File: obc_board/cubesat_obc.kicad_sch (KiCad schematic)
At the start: 16 parts

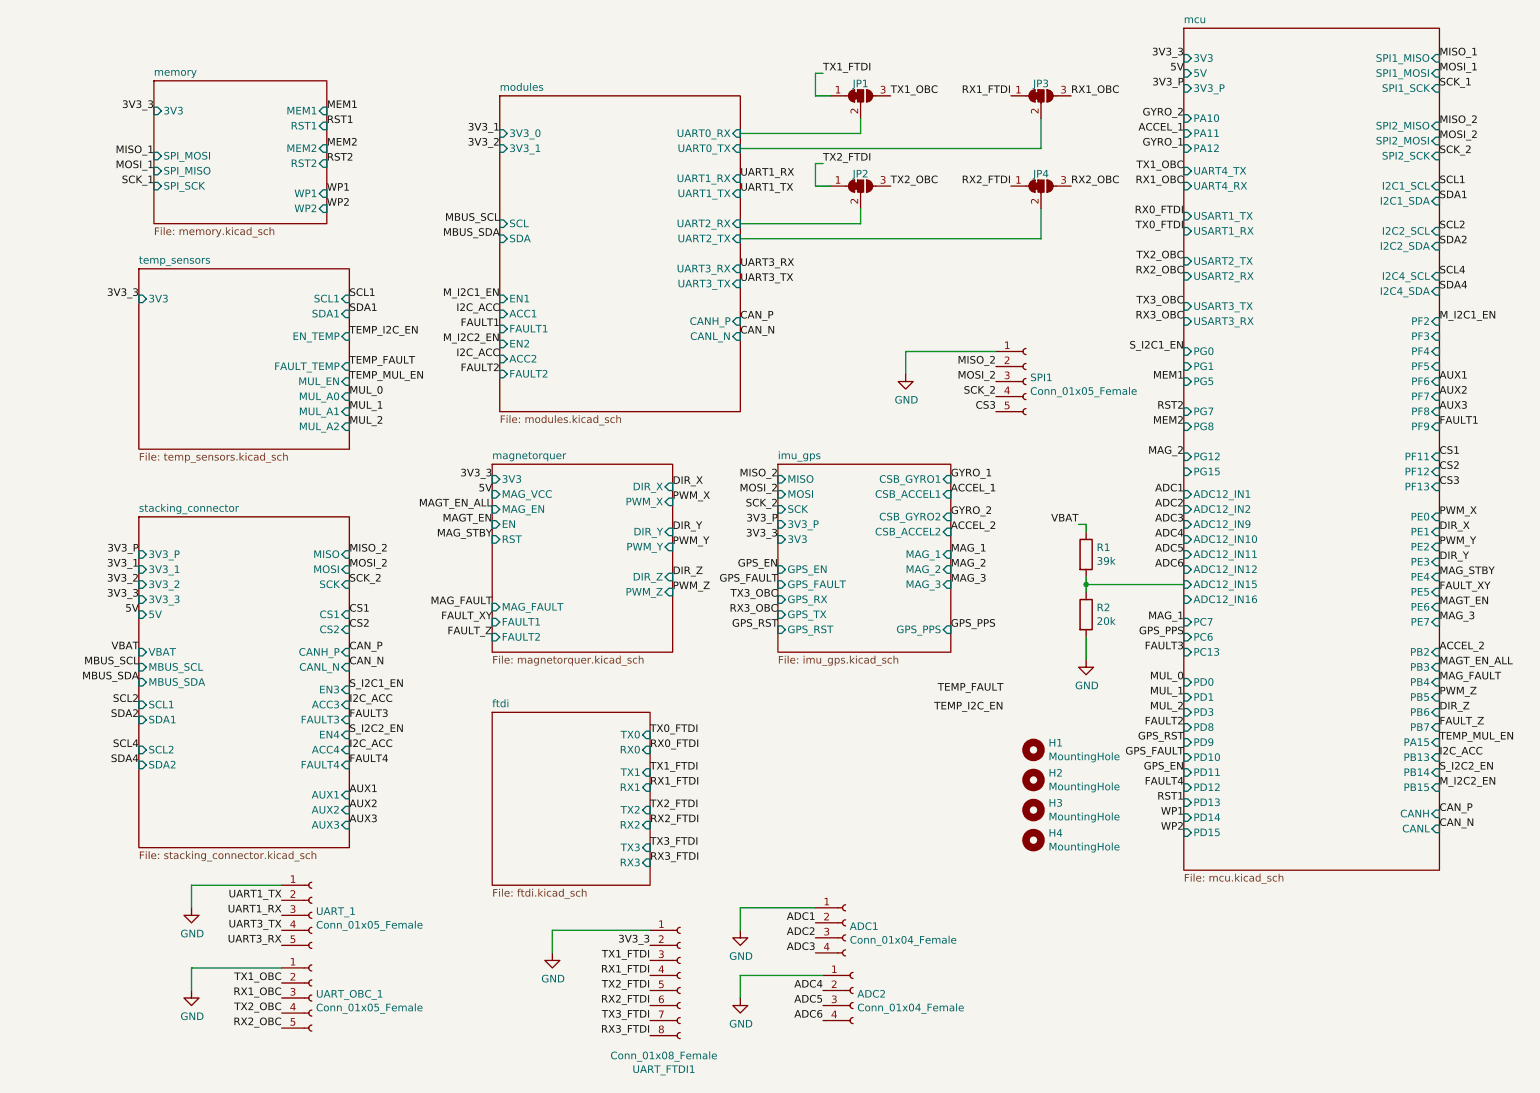
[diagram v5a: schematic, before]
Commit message: added silkscreen labels and gerber file
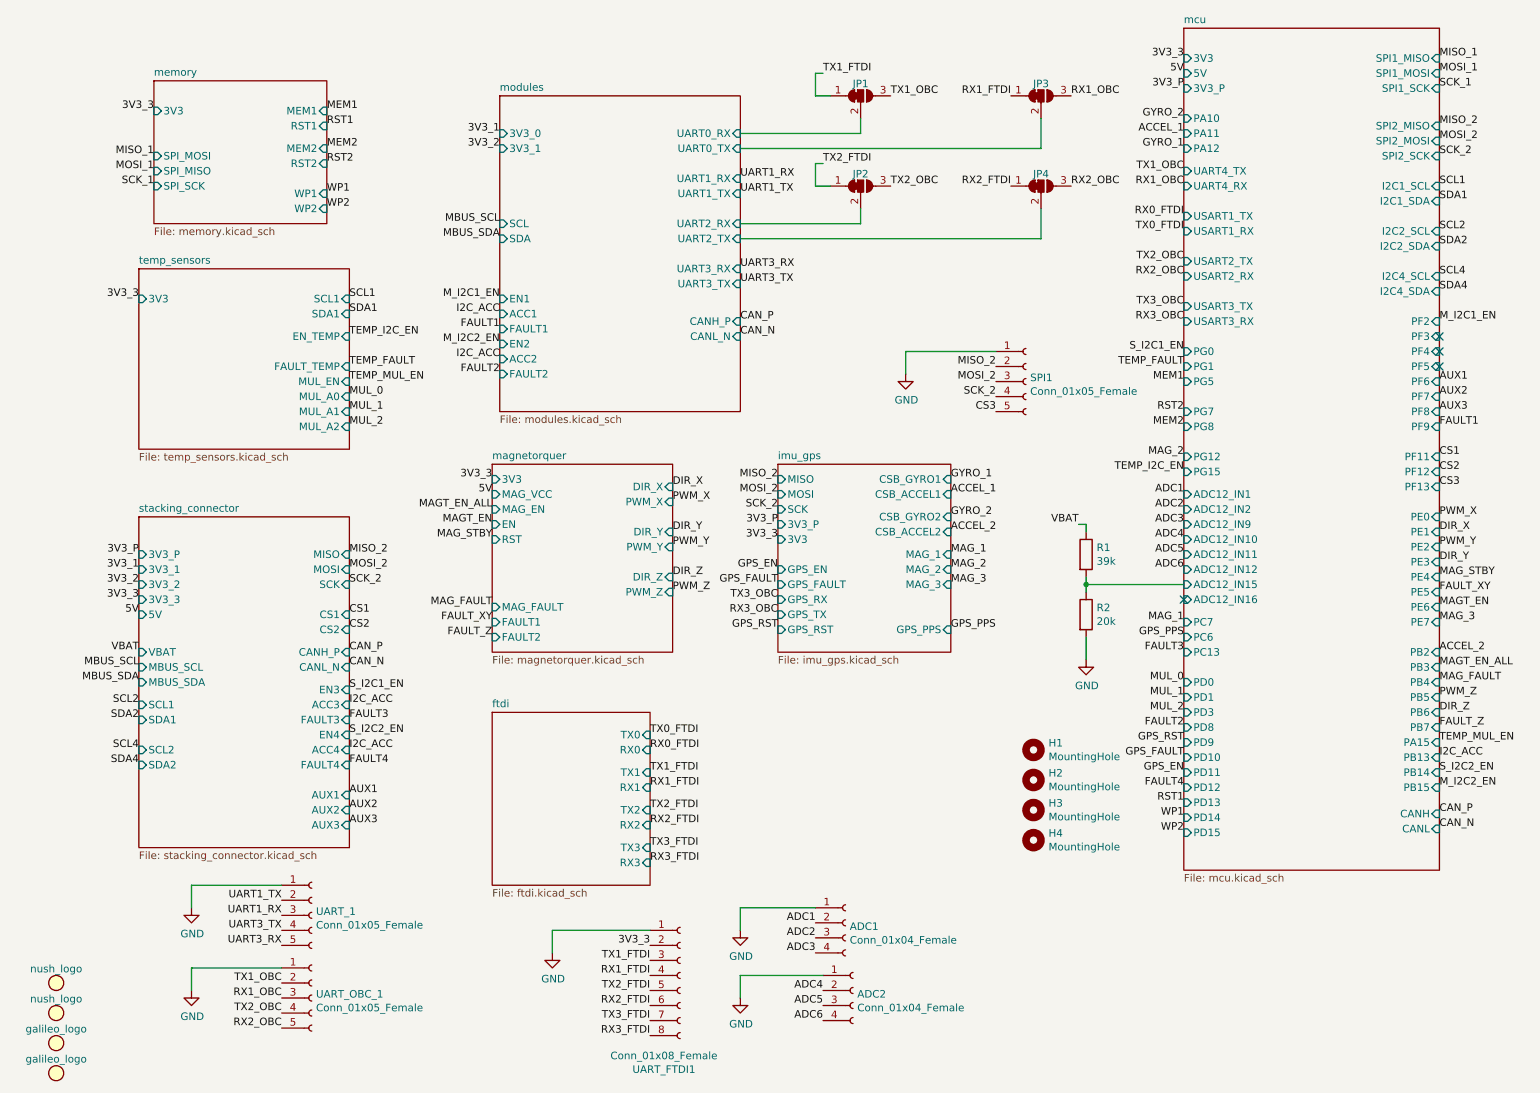
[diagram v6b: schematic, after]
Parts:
- added LOGO1, LOGO3: nush_logo, cubesat_obc:nush, symbol cubesat_obc_lib:nush_logo
- added LOGO2, LOGO4: galileo_logo, cubesat_obc:logo, symbol cubesat_obc_lib:galileo_logo
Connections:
- no-connect marks 0 -> 4
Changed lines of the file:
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@@
   (junction (at 194.31 111.76) (diameter 0) (color 0 0 0 0)
   )
+  (no_connect (at 210.82 114.3))
+  (no_connect (at 254 69.85))
+  (no_connect (at 254 72.39))
+  (no_connect (at 254 74.93))
   (wire (pts (xy 186.69 53.34) (xy 186.69 48.26))
     (stroke (width 0) (type default) (color 0 0 0 0))
@@
     (effects (font (size 1.27 1.27)) (justify right bottom))
   )
-  (label "TEMP_I2C_EN" (at 180.34 133.35 180)
+  (label "TEMP_I2C_EN" (at 210.82 92.71 180)
     (effects (font (size 1.27 1.27)) (justify right bottom))
   )
@@
     (effects (font (size 1.27 1.27)) (justify left bottom))
   )
-  (label "TEMP_FAULT" (at 180.34 130.175 180)
+  (label "TEMP_FAULT" (at 210.82 74.93 180)
     (effects (font (size 1.27 1.27)) (justify right bottom))
   )
@@
     (pin "1")
   )
+  (symbol (lib_id "cubesat_obc_lib:galileo_logo") (at 20.32 193.04 0) (unit 1)
+    (in_bom no) (on_board yes) (fields_autoplaced)
+    (property "Reference" "LOGO4" (id 0) (at 20.32 189.391 0)
+      (effects (font (size 1.27 1.27)) hide)
+    )
+    (property "Value" "galileo_logo" (id 1) (at 20.32 191.928 0))
+    (property "Footprint" "cubesat_obc:logo" (id 2) (at 20.32 193.04 0)
+      (effects (font (size 1.27 1.27)) hide)
+    )
+    (property "Datasheet" "" (id 3) (at 20.32 193.04 0)
+      (effects (font (size 1.27 1.27)) hide)
+    )
+  )
+  (symbol (lib_id "cubesat_obc_lib:galileo_logo") (at 20.32 187.96 0) (unit 1)
+    (in_bom no) (on_board yes) (fields_autoplaced)
+    (property "Reference" "LOGO2" (id 0) (at 20.32 184.311 0)
+      (effects (font (size 1.27 1.27)) hide)
+    )
+    (property "Value" "galileo_logo" (id 1) (at 20.32 186.848 0))
+    (property "Footprint" "cubesat_obc:logo" (id 2) (at 20.32 187.96 0)
+      (effects (font (size 1.27 1.27)) hide)
+    )
+    (property "Datasheet" "" (id 3) (at 20.32 187.96 0)
+      (effects (font (size 1.27 1.27)) hide)
+    )
+  )
   (symbol (lib_id "Jumper:SolderJumper_3_Bridged12") (at 186.69 44.45 0) (unit 1)
     (in_bom yes) (on_board yes) (fields_autoplaced)
@@
     )
     (pin "1")
+  )
+  (symbol (lib_id "cubesat_obc_lib:nush_logo") (at 20.32 176.53 0) (unit 1)
+    (in_bom no) (on_board yes) (fields_autoplaced)
+    (property "Reference" "LOGO3" (id 0) (at 20.32 174.151 0)
+      (effects (font (size 1.27 1.27)) hide)
+    )
+    (property "Value" "nush_logo" (id 1) (at 20.32 176.688 0))
+    (property "Footprint" "cubesat_obc:nush" (id 2) (at 20.32 176.53 0)
+      (effects (font (size 1.27 1.27)) hide)
+    )
+    (property "Datasheet" "" (id 3) (at 20.32 176.53 0)
+      (effects (font (size 1.27 1.27)) hide)
+    )
   )
   (symbol (lib_id "Connector:Conn_01x05_Female") (at 63.5 167.64 0) (unit 1)
@@
     )
     (pin "1")
+  )
+  (symbol (lib_id "cubesat_obc_lib:nush_logo") (at 20.32 181.61 0) (unit 1)
+    (in_bom no) (on_board yes) (fields_autoplaced)
+    (property "Reference" "LOGO1" (id 0) (at 20.32 179.231 0)
+      (effects (font (size 1.27 1.27)) hide)
+    )
+    (property "Value" "nush_logo" (id 1) (at 20.32 181.768 0))
+    (property "Footprint" "cubesat_obc:nush" (id 2) (at 20.32 181.61 0)
+      (effects (font (size 1.27 1.27)) hide)
+    )
+    (property "Datasheet" "" (id 3) (at 20.32 181.61 0)
+      (effects (font (size 1.27 1.27)) hide)
+    )
   )
   (symbol (lib_id "Connector:Conn_01x05_Female") (at 63.5 181.61 0) (unit 1)
@@
       (reference "L6") (unit 1) (value "4.7u") (footprint "cubesat_obc:L_Vishay_IHLP-2020")
     )
+    (path "/fd5bed97-1b44-4b26-b8b2-67238196ac4f"
+      (reference "LOGO1") (unit 1) (value "nush_logo") (footprint "cubesat_obc:nush")
+    )
+    (path "/2e22cb94-26aa-4819-a6b5-19b2eaba2a2a"
+      (reference "LOGO2") (unit 1) (value "galileo_logo") (footprint "cubesat_obc:logo")
+    )
+    (path "/c714194e-1b34-4b4e-883a-ced05fbeb8ae"
+      (reference "LOGO3") (unit 1) (value "nush_logo") (footprint "cubesat_obc:nush")
+    )
+    (path "/096e2b37-d7ae-49d5-8b8c-a245ea71385c"
+      (reference "LOGO4") (unit 1) (value "galileo_logo") (footprint "cubesat_obc:logo")
+    )
     (path "/00000000-0000-0000-0000-00005fc7207b/00000000-0000-0000-0000-00005fc87580"
       (reference "MAG_1") (unit 1) (value "Conn_01x02_Female") (footprint "Connector_Molex:Molex_PicoBlade_53261-0271_1x02-1MP_P1.25mm_Horizontal")
@@
       (reference "TP1") (unit 1) (value "MCO") (footprint "TestPoint:TestPoint_Pad_D1.5mm")
     )
+    (path "/00000000-0000-0000-0000-00005e7ec636/807784ee-2c9b-44bb-b95d-1f44a303a888"
+      (reference "TP?") (unit 1) (value "LSCO") (footprint "TestPoint:TestPoint_Pad_D1.5mm")
+    )
     (path "/00000000-0000-0000-0000-00005f315fb6/00000000-0000-0000-0000-00005f752a48"

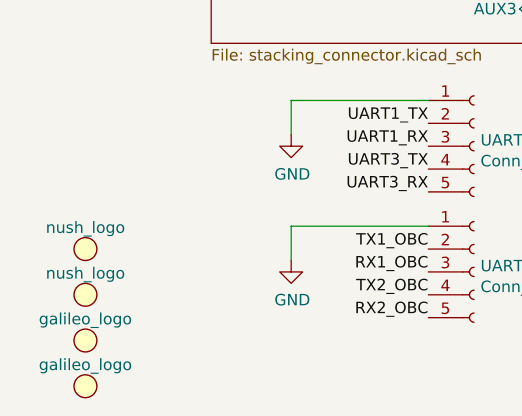
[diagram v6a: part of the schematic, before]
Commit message: added coordinate labels
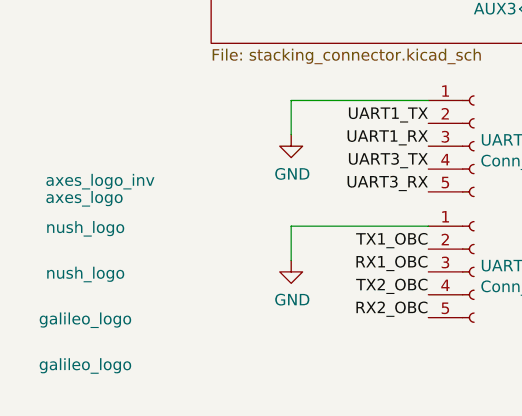
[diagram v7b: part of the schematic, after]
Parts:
- added LOGO5: axes_logo, cubesat_obc:axes, symbol cubesat_obc_lib:axes_logo
- added LOGO6: axes_logo_inv, cubesat_obc:axes_inv, symbol cubesat_obc_lib:axes_logo
- H1, H2, H3, H4, JP1, JP2, JP3, JP4: now left out of the parts list
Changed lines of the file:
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@@
   )
   (symbol (lib_id "Mechanical:MountingHole") (at 185.42 149.86 0) (unit 1)
-    (in_bom yes) (on_board yes)
+    (in_bom no) (on_board yes)
     (property "Reference" "H3" (id 0) (at 187.96 148.6916 0)
       (effects (font (size 1.27 1.27)) (justify left))
@@
   )
   (symbol (lib_id "Mechanical:MountingHole") (at 185.42 154.94 0) (unit 1)
-    (in_bom yes) (on_board yes)
+    (in_bom no) (on_board yes)
     (property "Reference" "H4" (id 0) (at 187.96 153.7716 0)
       (effects (font (size 1.27 1.27)) (justify left))
@@
   )
   (symbol (lib_id "Mechanical:MountingHole") (at 185.42 144.78 0) (unit 1)
-    (in_bom yes) (on_board yes)
+    (in_bom no) (on_board yes)
     (property "Reference" "H2" (id 0) (at 187.96 143.6116 0)
       (effects (font (size 1.27 1.27)) (justify left))
@@
   )
   (symbol (lib_id "Mechanical:MountingHole") (at 185.42 139.7 0) (unit 1)
-    (in_bom yes) (on_board yes)
+    (in_bom no) (on_board yes)
     (property "Reference" "H1" (id 0) (at 187.96 138.5316 0)
       (effects (font (size 1.27 1.27)) (justify left))
@@
     (pin "1")
   )
-  (symbol (lib_id "cubesat_obc_lib:galileo_logo") (at 20.32 193.04 0) (unit 1)
+  (symbol (lib_name "galileo_logo_1") (lib_id "cubesat_obc_lib:galileo_logo") (at 20.32 193.04 0) (unit 1)
     (in_bom no) (on_board yes) (fields_autoplaced)
     (property "Reference" "LOGO4" (id 0) (at 20.32 189.391 0)
@@
   )
   (symbol (lib_id "Jumper:SolderJumper_3_Bridged12") (at 186.69 44.45 0) (unit 1)
-    (in_bom yes) (on_board yes) (fields_autoplaced)
+    (in_bom no) (on_board yes) (fields_autoplaced)
     (property "Reference" "JP4" (id 0) (at 186.69 42.3982 0))
     (property "Value" "SolderJumper_3_Bridged12" (id 1) (at 186.69 42.3981 0)
@@
   )
   (symbol (lib_id "Jumper:SolderJumper_3_Bridged12") (at 156.21 44.45 0) (unit 1)
-    (in_bom yes) (on_board yes) (fields_autoplaced)
+    (in_bom no) (on_board yes) (fields_autoplaced)
     (property "Reference" "JP2" (id 0) (at 156.21 42.3982 0))
     (property "Value" "SolderJumper_3_Bridged12" (id 1) (at 156.21 42.3981 0)
@@
     (pin "3")
   )
+  (symbol (lib_id "cubesat_obc_lib:axes_logo") (at 20.32 173.355 0) (unit 1)
+    (in_bom no) (on_board yes)
+    (property "Reference" "LOGO5" (id 0) (at 21.59 172.0849 0)
+      (effects (font (size 1.27 1.27)) (justify left) hide)
+    )
+    (property "Value" "axes_logo" (id 1) (at 15.875 173.355 0)
+      (effects (font (size 1.27 1.27)) (justify left))
+    )
+    (property "Footprint" "cubesat_obc:axes" (id 2) (at 20.32 173.355 0)
+      (effects (font (size 1.27 1.27)) hide)
+    )
+    (property "Datasheet" "" (id 3) (at 20.32 173.355 0)
+      (effects (font (size 1.27 1.27)) hide)
+    )
+  )
   (symbol (lib_id "Jumper:SolderJumper_3_Bridged12") (at 156.21 29.21 0) (unit 1)
-    (in_bom yes) (on_board yes) (fields_autoplaced)
+    (in_bom no) (on_board yes) (fields_autoplaced)
     (property "Reference" "JP1" (id 0) (at 156.21 27.1582 0))
     (property "Value" "SolderJumper_3_Bridged12" (id 1) (at 156.21 27.1581 0)
@@
   )
   (symbol (lib_id "Jumper:SolderJumper_3_Bridged12") (at 186.69 29.21 0) (unit 1)
-    (in_bom yes) (on_board yes) (fields_autoplaced)
+    (in_bom no) (on_board yes) (fields_autoplaced)
     (property "Reference" "JP3" (id 0) (at 186.69 27.1582 0))
     (property "Value" "SolderJumper_3_Bridged12" (id 1) (at 186.69 27.1581 0)
@@
     (pin "1")
   )
-  (symbol (lib_id "cubesat_obc_lib:nush_logo") (at 20.32 176.53 0) (unit 1)
+  (symbol (lib_id "cubesat_obc_lib:axes_logo") (at 20.32 171.45 0) (unit 1)
+    (in_bom no) (on_board yes)
+    (property "Reference" "LOGO6" (id 0) (at 21.59 170.1799 0)
+      (effects (font (size 1.27 1.27)) (justify left) hide)
+    )
+    (property "Value" "axes_logo_inv" (id 1) (at 15.875 171.45 0)
+      (effects (font (size 1.27 1.27)) (justify left))
+    )
+    (property "Footprint" "cubesat_obc:axes_inv" (id 2) (at 20.32 171.45 0)
+      (effects (font (size 1.27 1.27)) hide)
+    )
+    (property "Datasheet" "" (id 3) (at 20.32 171.45 0)
+      (effects (font (size 1.27 1.27)) hide)
+    )
+  )
+  (symbol (lib_name "nush_logo_1") (lib_id "cubesat_obc_lib:nush_logo") (at 20.32 176.53 0) (unit 1)
     (in_bom no) (on_board yes) (fields_autoplaced)
     (property "Reference" "LOGO3" (id 0) (at 20.32 174.151 0)
@@
       (reference "LOGO4") (unit 1) (value "galileo_logo") (footprint "cubesat_obc:logo")
     )
+    (path "/4b138dbc-242e-4186-adee-f1b2ccf36379"
+      (reference "LOGO5") (unit 1) (value "axes_logo") (footprint "cubesat_obc:axes")
+    )
+    (path "/b98a0685-79cd-4074-bdb1-918f7563f4f8"
+      (reference "LOGO6") (unit 1) (value "axes_logo_inv") (footprint "cubesat_obc:axes_inv")
+    )
     (path "/00000000-0000-0000-0000-00005fc7207b/00000000-0000-0000-0000-00005fc87580"
       (reference "MAG_1") (unit 1) (value "Conn_01x02_Female") (footprint "Connector_Molex:Molex_PicoBlade_53261-0271_1x02-1MP_P1.25mm_Horizontal")
@@
     )
     (path "/00000000-0000-0000-0000-00005e7ec636/807784ee-2c9b-44bb-b95d-1f44a303a888"
-      (reference "TP?") (unit 1) (value "LSCO") (footprint "TestPoint:TestPoint_Pad_D1.5mm")
+      (reference "TP2") (unit 1) (value "LSCO") (footprint "TestPoint:TestPoint_Pad_D1.5mm")
     )
     (path "/00000000-0000-0000-0000-00005f315fb6/00000000-0000-0000-0000-00005f752a48"

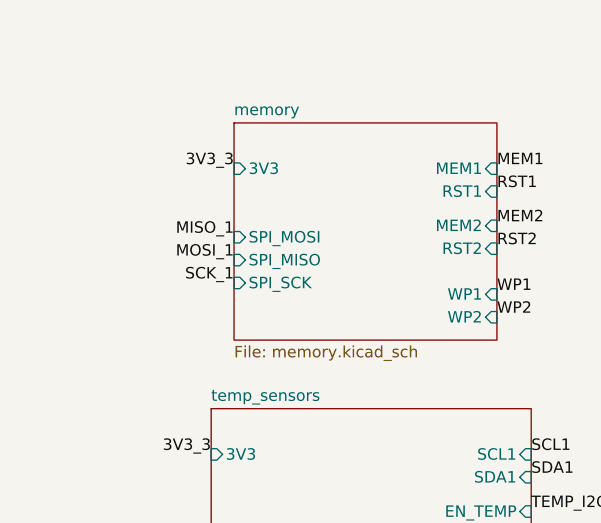
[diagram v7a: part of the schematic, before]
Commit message: fixed SPI pins mixup for memory, switched to MRAM instead of FRAM
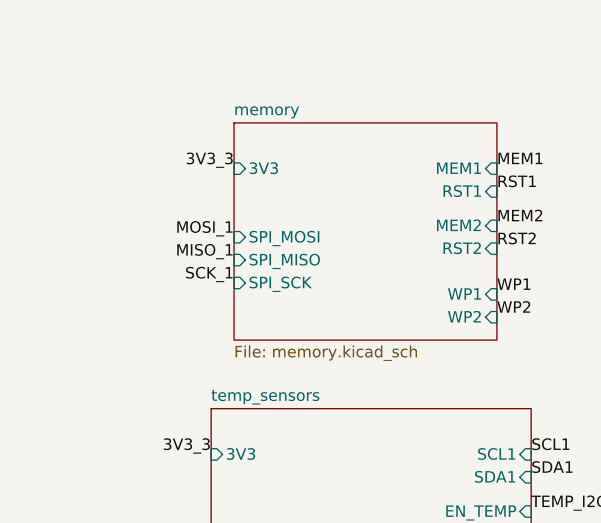
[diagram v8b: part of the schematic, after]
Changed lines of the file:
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@@
     (effects (font (size 1.27 1.27)) (justify right bottom))
   )
-  (label "MOSI_1" (at 36.83 41.91 180)
+  (label "MOSI_1" (at 36.83 39.37 180)
     (effects (font (size 1.27 1.27)) (justify right bottom))
   )
@@
     (effects (font (size 1.27 1.27)) (justify left bottom))
   )
-  (label "MISO_1" (at 36.83 39.37 180)
+  (label "MISO_1" (at 36.83 41.91 180)
     (effects (font (size 1.27 1.27)) (justify right bottom))
   )
@@
       (reference "#PWR057") (unit 1) (value "GND") (footprint "")
     )
+    (path "/00000000-0000-0000-0000-00005f3b62a5/7f358ec6-0177-4587-9400-0817dff2d3da"
+      (reference "#PWR058") (unit 1) (value "GND") (footprint "")
+    )
     (path "/00000000-0000-0000-0000-00005fc7207b/8458883a-5734-4709-8094-694631f54199"
       (reference "#PWR059") (unit 1) (value "GND") (footprint "")
@@
       (reference "U8") (unit 1) (value "IS25LE01G") (footprint "cubesat_obc:TFBGA24_5X5_6X8")
     )
-    (path "/00000000-0000-0000-0000-00005f3b62a5/3282b9b3-d336-4c2a-a96f-408357593b1b"
-      (reference "U9") (unit 1) (value "MB85RS2MLY") (footprint "Package_SO:SOIC-8_3.9x4.9mm_P1.27mm")
+    (path "/00000000-0000-0000-0000-00005f3b62a5/eb7659a8-7af1-4071-ab73-2c7d1a0c3e71"
+      (reference "U9") (unit 1) (value "MR25H40DF") (footprint "Package_DFN_QFN:DFN-8-1EP_6x5mm_P1.27mm_EP2x2mm")
     )
     (path "/00000000-0000-0000-0000-00005f3f9d17/00000000-0000-0000-0000-00005f4056a6"
